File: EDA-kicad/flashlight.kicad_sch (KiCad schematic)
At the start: 3 parts, among them U10 Flash-LED-Lumiled

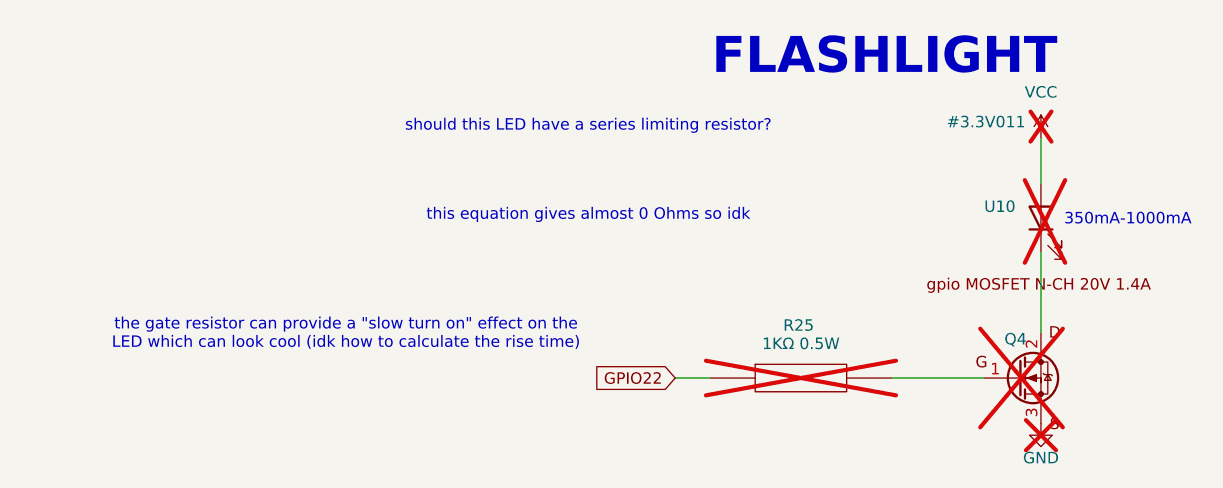
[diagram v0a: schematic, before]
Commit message: reannotate entire schematic
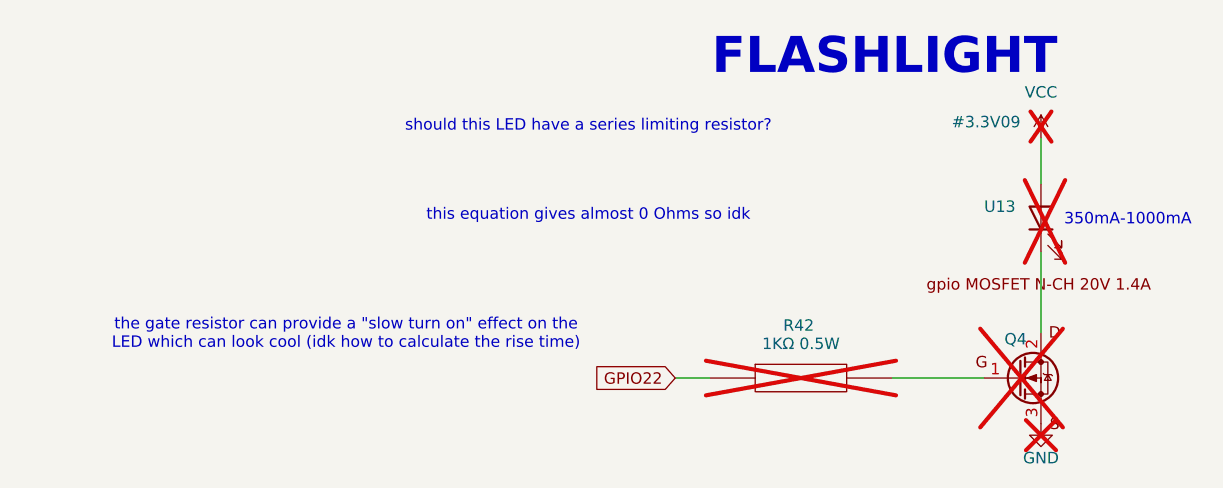
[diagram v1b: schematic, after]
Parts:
- renumbered R25 to R42, U10 to U13
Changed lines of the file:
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@@
 			"AAAAAAAAAAAAAAAAAAAAAAAAAAAAAAAAAAAAAAAAAAAAAAAAAAAAAAAAAAAAAAAAAAAAAAAAAAAA"
 			"AAAAAAAAAAAAAAAAAAAAAAAAAAAAAAAAAAAAAAAAAAAAAAAAAAAAAAAAAAAAAAAAAAAAAAAAAAAA"
-			"AAAAAAAAAAAAAAAAAA=="
+			"AAAAAAAAAAAAAAAAAAAAAAAAAAAAAAAAAAAAAAAAAAAAAAAAAAAAAAAAgHacqNZVAAAsAAAAAAAA"
+			"ACwAAAAAAAAAMHicqNZVAAAAAAAAAAAAAAAAAAAAAAAAkMb0mtZVAACAxvSa1lUAAAEAAAACAAAA"
+			"gL2cqNZVAABxAgAAAAAAANDWnKjWVQAAsGqcqNZVAABuAAAAbgAAAGUAAABjAAAAdAAAAGUAAABk"
+			"AAAALQAAACgAAABNAAAAbwAAAGQAAAB1AAAAbAAAAGUAAAAxAAAAQQAAAC0AAABFAAAAdAAAAGgA"
+			"AABlAAAAcgAAAG4AAABlAAAAdAAAAF8AAABQAAAAYQAAAGkAAAByAAAAMwAAAF8AAABQAAAALQAA"
+			"AFAAAABhAAAAZAAAADMAAAApAAAAAAAAAFMAAACxAQAAAAAAANDWnKjWVQAAwBw/Agd/AABuAAAA"
+			"bgAAAGUAAABjAAAAdAAAAGUAAABkAAAALQAAACgAAABNAAAAbwAAAGQAAAB1AAAAbAAAAGUAAAAx"
+			"AAAAQQAAAC0AAABFAAAAdAAAAGgAAABlAAAAcgAAAG4AAABlAAAAdAAAAF8AAABQAAAAYQAAAGkA"
+			"AAByAAAAMQAAAF8AAABOAAAALQAAAFAAAABhAAAAZAAAADYAAAApAAAAwAAAAAAAAADAAAAAAAAA"
+			"AHUAAABuAAAAYwAAAG8AAABuAAAAbgAAAGUAAABjAAAAdAAAAGUAAABkAAAALQAAACgAAABNAAAA"
+			"bwAAAGQAAAB1AAAAbAAAAGUAAAAxAAAAQQAAAC0AAABFAAAAdAAAAGgAAABlAAAAcgAAAG4AAABl"
+			"AAAAdAAAAF8AAABQAAAAYQAAAGkAAAByAAAAMwAAAF8AAABQAAAALQAAAFAAAABhAAAAZAAAADMA"
+			"AAApAAAAAAAAAAAAAAAxAAAAAAAAALDyn6jWVQAAUFygqNZVAACTp7ABuSgZB+BznKjWVQAAkAMA"
+			"AAAAAADAAAAAAAAAAHUAAABuAAAAYwAAAG8AAABuAAAAbgAAAGUAAABjAAAAdAAAAGUAAABkAAAA"
+			"LQAAACgAAABNAAAAbwAAAGQAAAB1AAAAbAAAAGUAAAAxAAAAQQAAAC0AAABFAAAAdAAAAGgAAABl"
+			"AAAAcgAAAG4AAABlAAAAdAAAAF8AAABQAAAAYQAAAGkAAAByAAAAMwAAAF8AAABQAAAALQAAAFAA"
+			"AABhAAAAZAAAADMAAAApAAAA8GEAAAAAAABAAAAAAAAAALf19vXTVQAAgHycqNZVAAAAAAAAAAAA"
+			"AAAAAAAAAAAAoA4BAAAAAABQAAAAAAAAAGfx9vXTVQAAQB7LBAd/AACgNban1lUAAFAhywQHfwAA"
+			"0Easp9ZVAADg88sEBw=="
 		)
 	)
@@
 		(on_board yes)
 		(dnp yes)
-		(property "Reference" "U10"
+		(property "Reference" "U13"
 			(at 165.608 85.09 90)
 			(effects
@@
 			(project "cm5-carrier"
 				(path "/28c5e4fe-1ec7-4477-97f0-d2ec1401fad5/b409b5f4-0f84-46c0-84e6-a0b4d149590c"
-					(reference "U10")
+					(reference "U13")
 					(unit 1)
 				)
@@
 		(on_board yes)
 		(dnp yes)
-		(property "Reference" "R25"
+		(property "Reference" "R42"
 			(at 143.256 98.298 0)
 			(effects
@@
 			(project "cm5-carrier"
 				(path "/28c5e4fe-1ec7-4477-97f0-d2ec1401fad5/b409b5f4-0f84-46c0-84e6-a0b4d149590c"
-					(reference "R25")
+					(reference "R42")
 					(unit 1)
 				)
@@
 		(on_board yes)
 		(dnp yes)
-		(property "Reference" "#3.3V011"
+		(property "Reference" "#3.3V09"
 			(at 164.084 75.692 0)
 			(effects
@@
 			(project "cm5-carrier"
 				(path "/28c5e4fe-1ec7-4477-97f0-d2ec1401fad5/b409b5f4-0f84-46c0-84e6-a0b4d149590c"
-					(reference "#3.3V011")
+					(reference "#3.3V09")
 					(unit 1)
 				)
@@
 		(on_board yes)
 		(dnp yes)
-		(property "Reference" "#PWR0130"
+		(property "Reference" "#PWR0148"
 			(at 170.18 115.57 0)
 			(effects
@@
 			(project "cm5-carrier"
 				(path "/28c5e4fe-1ec7-4477-97f0-d2ec1401fad5/b409b5f4-0f84-46c0-84e6-a0b4d149590c"
-					(reference "#PWR0130")
+					(reference "#PWR0148")
 					(unit 1)
 				)
